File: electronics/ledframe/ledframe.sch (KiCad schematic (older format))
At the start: 25 parts, among them CON1 BARREL_JACK, CON2 SD_Card, IC1 ATMEGA328P-AUR, P1 PIEZO_IN, P2 CONN_01X06, P3 ICSP, P4 LED_WS2812b, P5 ANT, Q1 BSS138, Q2 BSS138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

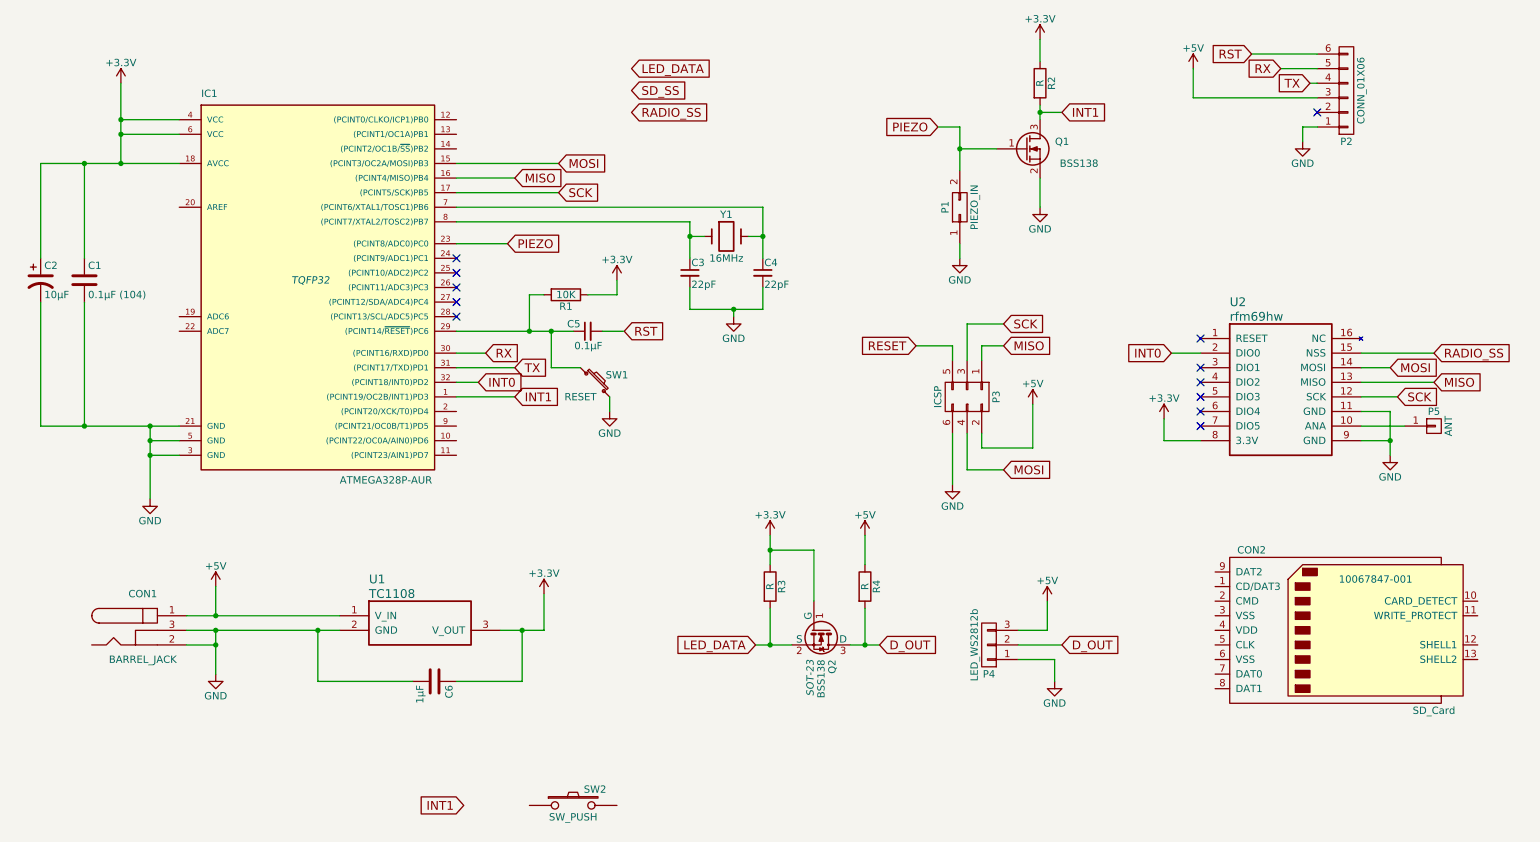
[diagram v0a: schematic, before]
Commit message: EOD: there's a circuit, but no board layout yet
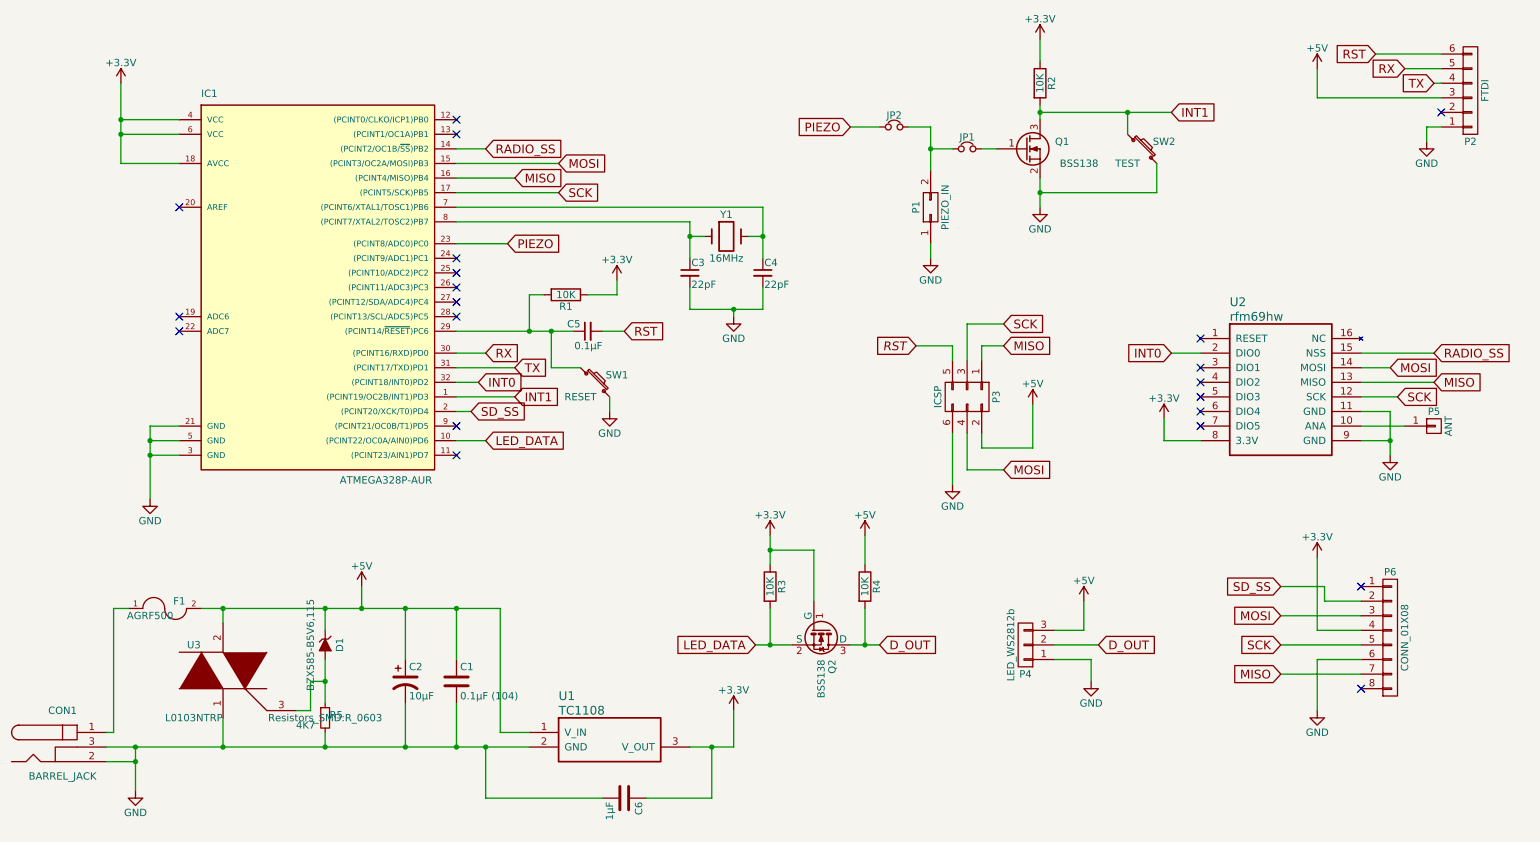
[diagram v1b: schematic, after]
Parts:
- removed CON2: SD_Card, 10067847-001, symbol SD_Card
- removed SW2: SW_PUSH, symbol SW_PUSH
- added D1: BZX585-B5V6,115, Diodes_SMD:SOD-523, symbol ZENERsmall
- added F1: AGRF500, Resistors_ThroughHole:Resistor_Horizontal_RM7mm, symbol FUSE
- added JP1, JP2: Jumper_NC_Small, local:NC_SMD_JPR, symbol Jumper_NC_Small
- added P6: CONN_01X08, local:MicroSD_Molex_47309, symbol CONN_01X08
- added R5: 4K7, Resistors_SMD:R_0603, symbol R_Small
- added SW2: TEST, local:KSEx00G_SW, symbol SW_PUSH_SMALL
- added U3: L0103NTRP, TO_SOT_Packages_SMD:SOT-223, symbol TRIAC
- C1, C3, C4, C5: footprint (none) -> Capacitors_SMD:C_0603
- C2: footprint (none) -> Capacitors_SMD:c_elec_3x5.3
- C6: footprint (none) -> Capacitors_SMD:C_0805
- CON1: footprint (none) -> Connect:BARREL_JACK
- IC1: footprint TQFP32 -> Housings_QFP:TQFP-32_7x7mm_Pitch0.8mm
- P1: footprint (none) -> Pin_Headers:Pin_Header_Straight_2x01
- P2: value CONN_01X06 -> FTDI; footprint (none) -> local:Pin_Header_Straight_1x06
- P3: footprint (none) -> Pin_Headers:Pin_Header_Straight_2x03
- P4: footprint (none) -> local:Pin_Header_Straight_1x03
- P5: footprint (none) -> Socket_Strips:Socket_Strip_Straight_1x01
- Q1: footprint (none) -> TO_SOT_Packages_SMD:SOT-23
- Q2: footprint SOT-23 -> TO_SOT_Packages_SMD:SOT-23
- R1: footprint (none) -> Resistors_SMD:R_0603
- R2, R3, R4: value R -> 10K; footprint (none) -> Resistors_SMD:R_0603
- SW1: footprint (none) -> local:KSEx00G_SW
- U1: footprint (none) -> TO_SOT_Packages_SMD:SOT-223
- U2: footprint (none) -> Housings_DIP:DIP-16_W7.62mm
- Y1: footprint (none) -> Crystals:Crystal_HC49-SD_SMD
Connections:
- net RESET is gone; now on net RST: P3.5 (P5)
- net +3V3: now also P6.4 (P4); no longer C1.1, C2.1
- net +5V: now also C1.1, C2.1, D1.1 (K), F1.2, U3.2; no longer CON1.1
- net GND: now also P6.6 (P6), R5.2, SW2.2, U3.1
- net INT1: now also SW2.1
- net LED_DATA: now also IC1.10 ((PCINT22/OC0A/AIN0)PD6)
- net MISO: now also P6.7 (P7)
- net MOSI: now also P6.3 (P3)
- net PIEZO: now also JP2.1; no longer P1.2 (P2), Q1.1 (G)
- net RADIO_SS: now also IC1.14 ((PCINT2/OC1B/~SS~)PB2)
- net SCK: now also P6.5 (P5)
- net SD_SS: now also IC1.2 ((PCINT20/XCK/T0)PD4), P6.2 (P2)
- new net: JP1.1, JP2.2, P1.2 (P2)
- new net: JP1.2, Q1.1 (G)
- new net: CON1.1, F1.1
- new net: D1.2 (A), R5.1, U3.3
- no-connect marks 12 -> 21
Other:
- moved on the sheet: C1, C2, C6, CON1, P1, P2, P4, U1

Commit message: changed to resonator
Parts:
- removed C3, C4: 22pF, Capacitors_SMD:C_0603, symbol C_Small
- removed Y1: 16MHz, Crystals:Crystal_HC49-SD_SMD, symbol Crystal
- added Y1: Resonator, Crystals:Resonator_7.2x3mm, symbol Resonator
- P6: value CONN_01X08 -> MicroSD
- renumbered C5 to C3, C6 to C4
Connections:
- net GND: now also Y1.2 (GND)
- net at IC1.7 ((PCINT6/XTAL1/TOSC1)PB6): now also Y1.3 (C2)
- net at IC1.8 ((PCINT7/XTAL2/TOSC2)PB7): now also Y1.1 (C1)
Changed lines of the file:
@@
 RST
 $Comp
-L C_Small C5
+L C_Small C3
 U 1 1 56D7602A
 P 4800 3050
-F 0 "C5" V 4850 3100 50  0000 L CNN
+F 0 "C3" V 4850 3100 50  0000 L CNN
 F 1 "0.1µF" V 4700 2950 50  0000 L CNN
 F 2 "Capacitors_SMD:C_0603" H 4800 3050 50  0001 C CNN
@@
 TX
 $Comp
-L Crystal Y1
-U 1 1 56D76665
-P 5750 2400
-F 0 "Y1" H 5750 2550 50  0000 C CNN
-F 1 "16MHz" H 5750 2250 50  0000 C CNN
-F 2 "Crystals:Crystal_HC49-SD_SMD" H 5750 2400 50  0001 C CNN
-F 3 "" H 5750 2400 50  0000 C CNN
-	1    5750 2400
-	1    0    0    -1
-$EndComp
-$Comp
-L C_Small C4
-U 1 1 56D76D8E
-P 6000 2650
-F 0 "C4" H 6010 2720 50  0000 L CNN
-F 1 "22pF" H 6010 2570 50  0000 L CNN
-F 2 "Capacitors_SMD:C_0603" H 6000 2650 50  0001 C CNN
-F 3 "" H 6000 2650 50  0000 C CNN
-	1    6000 2650
-	1    0    0    -1
-$EndComp
-$Comp
-L C_Small C3
-U 1 1 56D76DBE
-P 5500 2650
-F 0 "C3" H 5510 2720 50  0000 L CNN
-F 1 "22pF" H 5510 2570 50  0000 L CNN
-F 2 "Capacitors_SMD:C_0603" H 5500 2650 50  0001 C CNN
-F 3 "" H 5500 2650 50  0000 C CNN
-	1    5500 2650
-	1    0    0    -1
-$EndComp
-$Comp
 L GND #PWR04
 U 1 1 56D76E77
-P 5800 2950
-F 0 "#PWR04" H 5800 2700 50  0001 C CNN
-F 1 "GND" H 5800 2800 50  0000 C CNN
-F 2 "" H 5800 2950 50  0000 C CNN
-F 3 "" H 5800 2950 50  0000 C CNN
-	1    5800 2950
+P 5850 3150
+F 0 "#PWR04" H 5850 2900 50  0001 C CNN
+F 1 "GND" H 5850 3000 50  0000 C CNN
+F 2 "" H 5850 3150 50  0000 C CNN
+F 3 "" H 5850 3150 50  0000 C CNN
+	1    5850 3150
 	1    0    0    -1
 $EndComp
@@
 $EndComp
 $Comp
-L C C6
+L C C4
 U 1 1 56D7D57D
 P 5050 6250
-F 0 "C6" H 5075 6350 50  0000 L CNN
+F 0 "C4" H 5075 6350 50  0000 L CNN
 F 1 "1µF" H 5075 6150 50  0000 L CNN
 F 2 "Capacitors_SMD:C_0805" H 5088 6100 50  0001 C CNN
@@
 F 0 "R5" H 3030 5720 50  0000 L CNN
 F 1 "4K7" H 2800 5650 50  0000 L CNN
-F 2 "Resistors_SMD:R_0603" H 3000 5700 50  0000 C CNN
+F 2 "Resistors_SMD:R_0603" H 3000 5700 50  0001 C CNN
 F 3 "" H 3000 5700 50  0000 C CNN
 	1    3000 5700
@@
 P 10300 5150
 F 0 "P6" H 10300 5600 50  0000 C CNN
-F 1 "CONN_01X08" V 10400 5150 50  0000 C CNN
+F 1 "MicroSD" V 10400 5150 50  0000 C CNN
 F 2 "local:MicroSD_Molex_47309" H 10300 5150 50  0001 C CNN
 F 3 "" H 10300 5150 50  0000 C CNN
@@
 	4550 3300 4750 3300
 Wire Wire Line
-	3900 2200 6000 2200
-Wire Wire Line
-	6000 2200 6000 2550
-Wire Wire Line
-	6000 2400 5900 2400
-Wire Wire Line
-	3900 2300 5500 2300
-Wire Wire Line
-	5500 2300 5500 2550
-Wire Wire Line
-	5500 2400 5600 2400
-Connection ~ 5500 2400
-Connection ~ 6000 2400
-Wire Wire Line
-	6000 2900 6000 2750
-Wire Wire Line
-	5500 2900 6000 2900
-Wire Wire Line
-	5500 2900 5500 2750
-Wire Wire Line
-	5800 2950 5800 2900
-Connection ~ 5800 2900
+	3900 2200 6250 2200
+Wire Wire Line
+	3900 2300 5450 2300
 Wire Wire Line
 	4250 2450 3900 2450
@@
 	4100 6250 4100 5900
 Connection ~ 4100 5900
+$Comp
+L Resonator Y1
+U 1 1 56F7E999
+P 5850 2350
+F 0 "Y1" H 6050 1650 60  0000 C CNN
+F 1 "Resonator" H 5850 2350 60  0000 C CNN
+F 2 "Crystals:Resonator_7.2x3mm" H 5850 2350 60  0001 C CNN
+F 3 "" H 5850 2350 60  0000 C CNN
+F 4 "CSTCE16M0V53Z-R0" H 5850 2350 60  0001 C CNN "manf#"
+	1    5850 2350
+	1    0    0    -1
+$EndComp
+Wire Wire Line
+	6250 2200 6250 2450
+Wire Wire Line
+	5450 2300 5450 2450
 $EndSCHEMATC

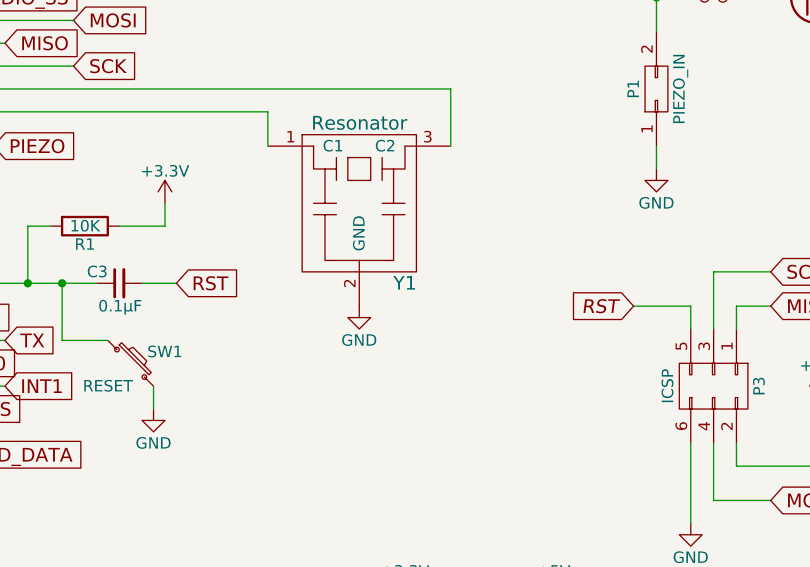
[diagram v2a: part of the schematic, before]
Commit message: included the missing resonator(!)
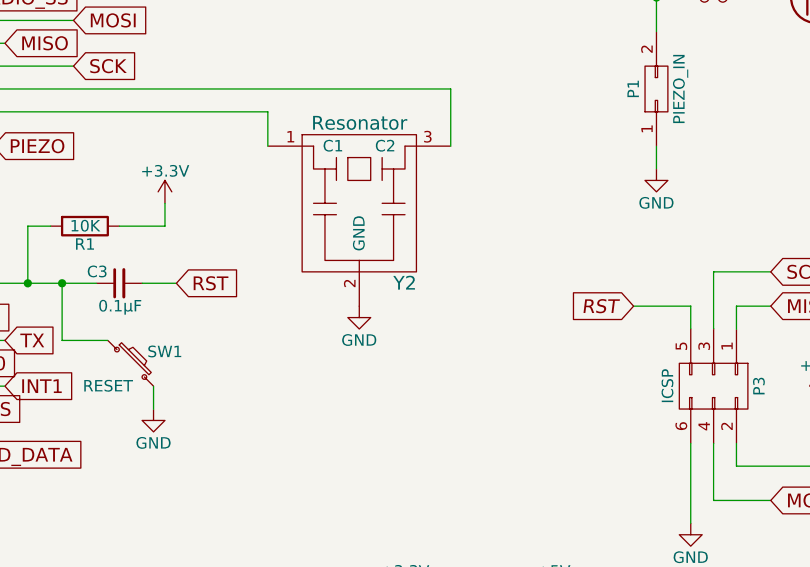
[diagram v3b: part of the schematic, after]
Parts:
- Y2: renamed from Y1; footprint Crystals:Resonator_7.2x3mm -> local:Resonator_3.2x1.3
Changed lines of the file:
@@
 Connection ~ 4100 5900
 $Comp
-L Resonator Y1
+L Resonator Y2
 U 1 1 56F7E999
 P 5850 2350
-F 0 "Y1" H 6050 1650 60  0000 C CNN
+F 0 "Y2" H 6050 1650 60  0000 C CNN
 F 1 "Resonator" H 5850 2350 60  0000 C CNN
-F 2 "Crystals:Resonator_7.2x3mm" H 5850 2350 60  0001 C CNN
+F 2 "local:Resonator_3.2x1.3" H 5850 2350 60  0001 C CNN
 F 3 "" H 5850 2350 60  0000 C CNN
 F 4 "CSTCE16M0V53Z-R0" H 5850 2350 60  0001 C CNN "manf#"
